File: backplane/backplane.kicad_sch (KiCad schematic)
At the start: 20 parts, among them J1 Conn_01x10, J10 Conn_01x10, J11 Conn_01x10, J2 Conn_01x10, J3 48V in, J4 48V in, J5 Conn_01x10, J6 Conn_01x10, J7 Conn_01x10, J8 Conn_01x10, J9 Conn_01x10

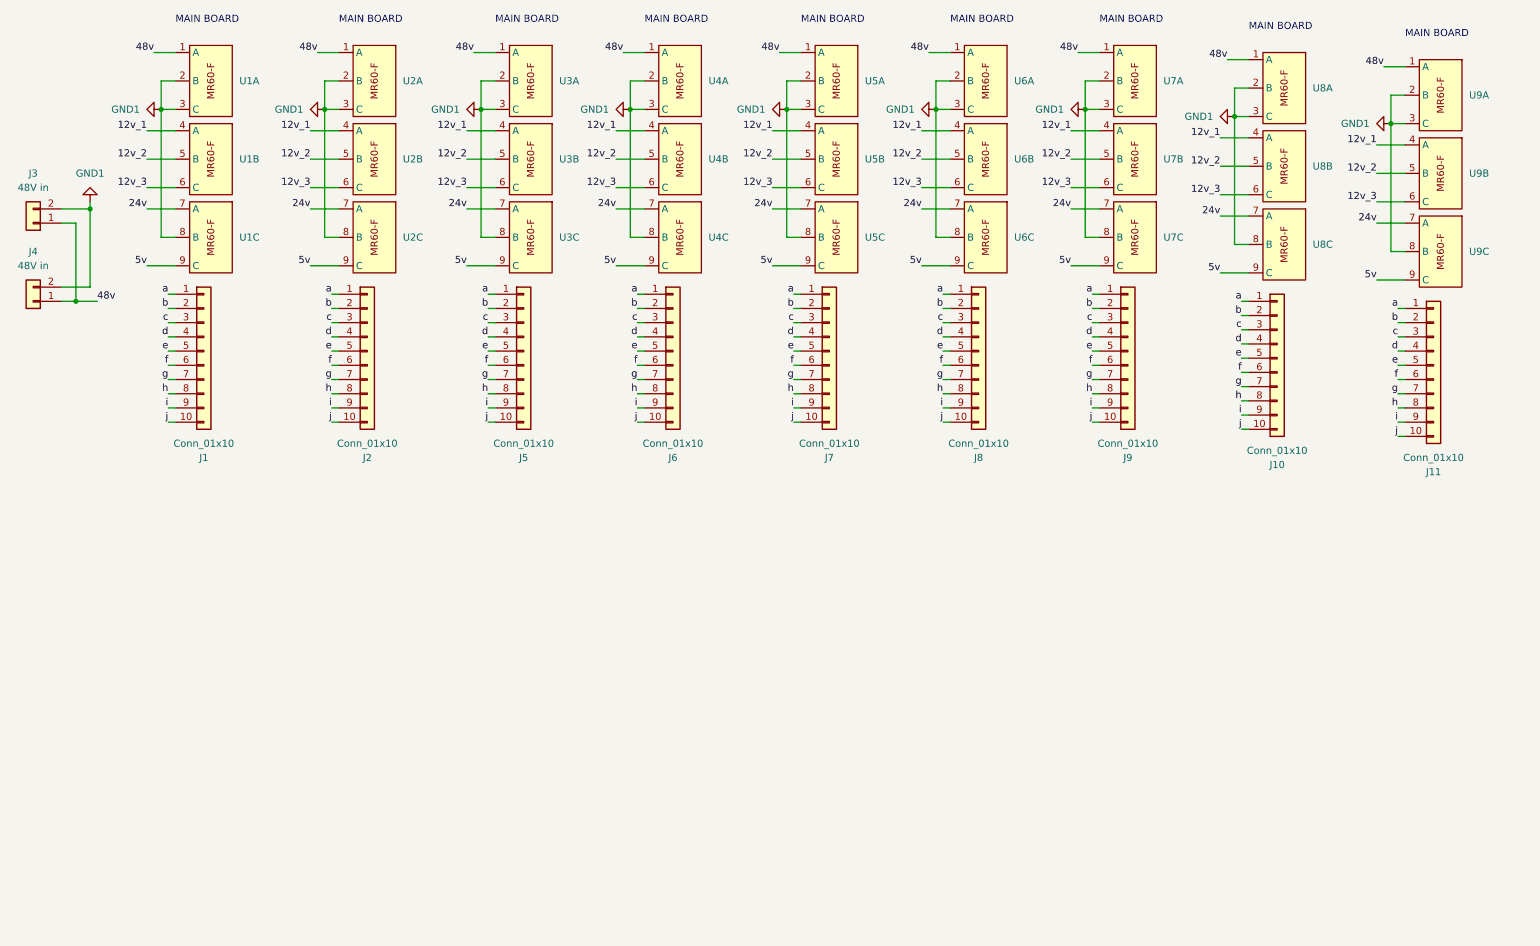
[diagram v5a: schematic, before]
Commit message: added links, tried to do a BOM, modified silkscreen
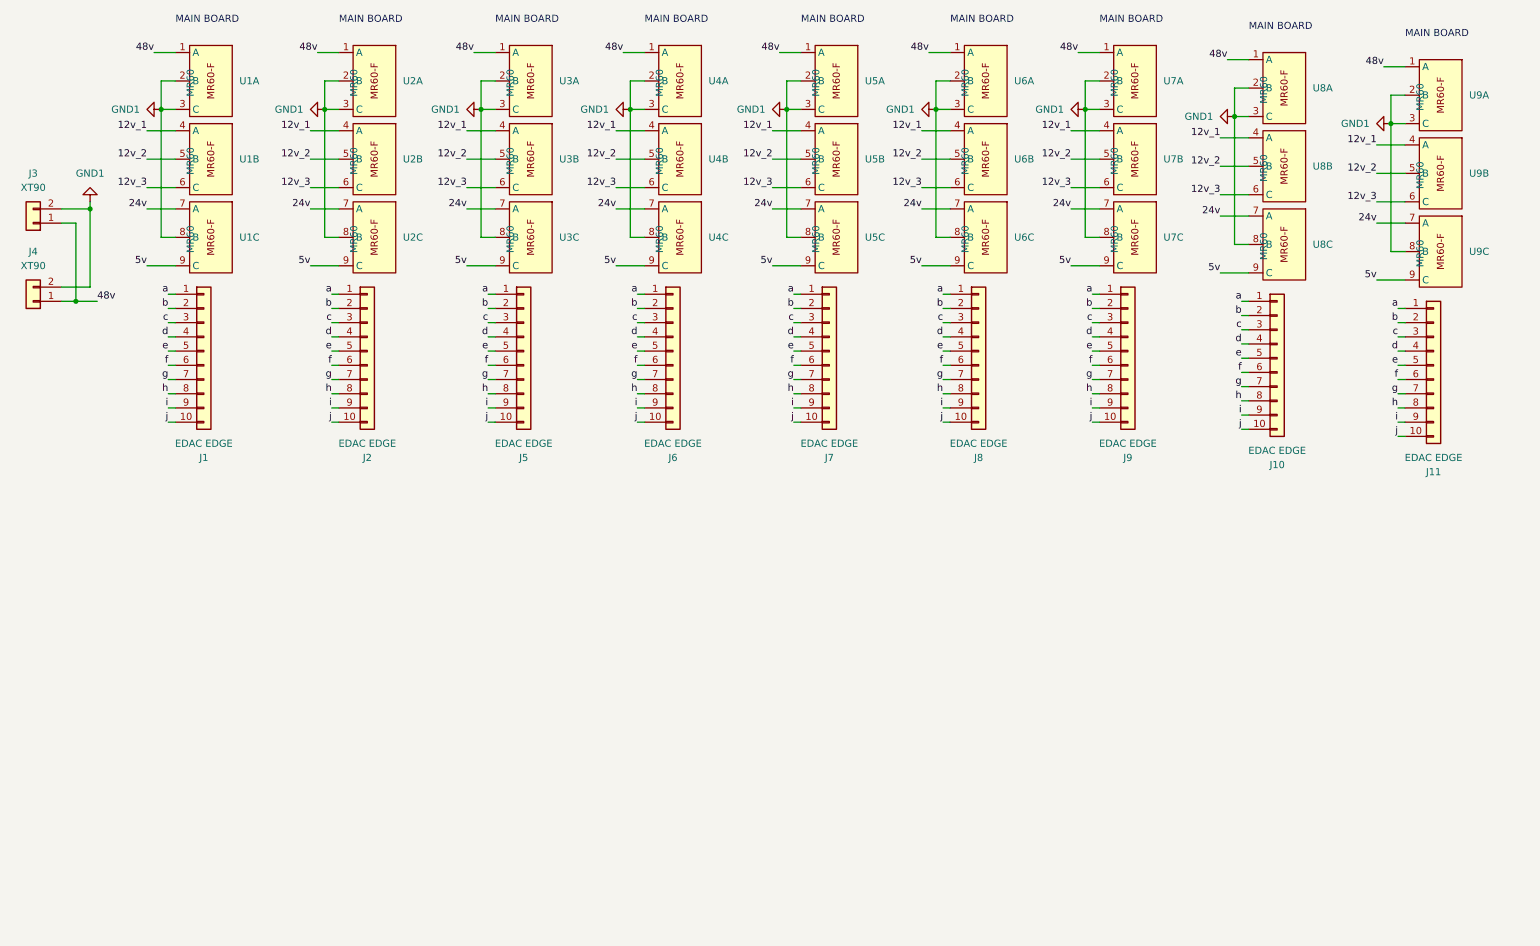
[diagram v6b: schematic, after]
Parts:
- J1, J10, J11, J2, J5, J6, J7, J8, J9: value Conn_01x10 -> EDAC EDGE; Link (none) -> https://www.digikey.ca/en/products/detail/edac-inc/341-020-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
- J3, J4: value 48V in -> XT90
- U1, U2, U3, U4, U5, U6, U7, U8, U9: value ~ -> MR60; Link (none) -> https://www.tme.com/ca/en/details/mr60pw-m/dc-power-connect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
